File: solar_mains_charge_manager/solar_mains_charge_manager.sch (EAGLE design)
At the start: 11 parts, among them T1 TIP122, X1 22-23-2031, X2 22-23-2021, X4 22-23-2031, X5 22-23-2031

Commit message: Some more schematic and spreadsheet
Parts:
- added C1: (no value), capacitor-wima:C5/2.5
- added D1, D2, D3, D4: 1N4004, diode:1N4004
- added D5: (no value), diode:ZENER-DIODEDO34-7
- added OK2: PC817, optocoupler:PC817
- added R5: (no value), resistor:R-EU_0204/5
- added R6, R7, R8: (no value), resistor:R-EU_0204/7
- added X3: 22-23-2031, con-molex:22-23-2031
- added X6: 22-23-2041, con-molex:22-23-2041
- added X7, X8: 53047-15, con-molex:53047-15
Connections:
- new net N$10: D3.A, D4.A, D5.A, OK2.C
- new net N$11: D1.C, D2.C, R7.2
- new net N$12: OK2.COL, U$1.D12, X8-1.S
- new net N$13: C1.1, D1.A, D3.C, R8.1
- new net N$14: C1.2, R8.2
- new net N$15: D2.A, D4.C, R6.1
- new net N$16: R6.2
- new net N$17: U$1.D11, X3-2.S, X8-2.S
- new net N$18: U$1.D10, X3-3.S, X8-3.S
- new net N$19: U$1.D9, X6-3.S, X8-4.S
- new net N$20: U$1.D8, X6-4.S, X8-5.S
- new net N$21: U$1.RST, X6-2.S, X7-3.S
- new net N$22: U$1.D7, X8-6.S
- new net N$23: U$1.D6, X8-7.S
- new net N$24: U$1.D5, X8-8.S
- new net N$25: U$1.D4, X8-9.S
- new net N$26: U$1.D3, X8-10.S
- new net N$27: U$1.D2, X8-11.S
- new net N$28: U$1.GND2, X8-12.S
- new net N$29: U$1.RST1, X8-13.S
- new net N$30: U$1.RX1, X8-14.S
- new net N$31: U$1.TX0, X8-15.S
- new net N$32: U$1.5.5V, X7-4.S
- new net N$33: U$1.A7, X7-5.S
- new net N$34: U$1.A6, X7-6.S
- new net N$35: U$1.A5, X7-7.S
- new net N$36: U$1.A4, X7-8.S
- new net N$37: U$1.A3, X7-9.S
- new net N$38: U$1.A2, X7-10.S
- new net N$39: U$1.A1, X7-11.S
- new net N$8: OK2.A, R5.1
- new net N$9: D5.C, R5.2, R7.1
- net 12V: now also X7-1.S
- net GND: now also OK2.EMIT, X3-1.S, X6-1.S, X7-2.S
- net N$1: now also X7-13.S, X7-14.S
- net N$2: now also X7-15.S
- net N$3: now also X7-12.S

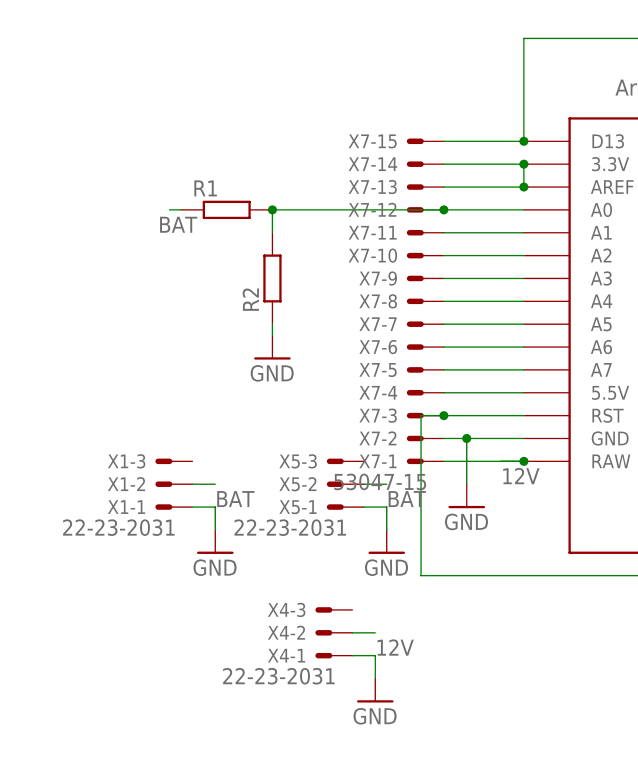
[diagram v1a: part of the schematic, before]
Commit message: Added solar panel voltage measurement along with over voltage and negative voltage protection in schematic, plus comments on the same in psu_considerations.ods
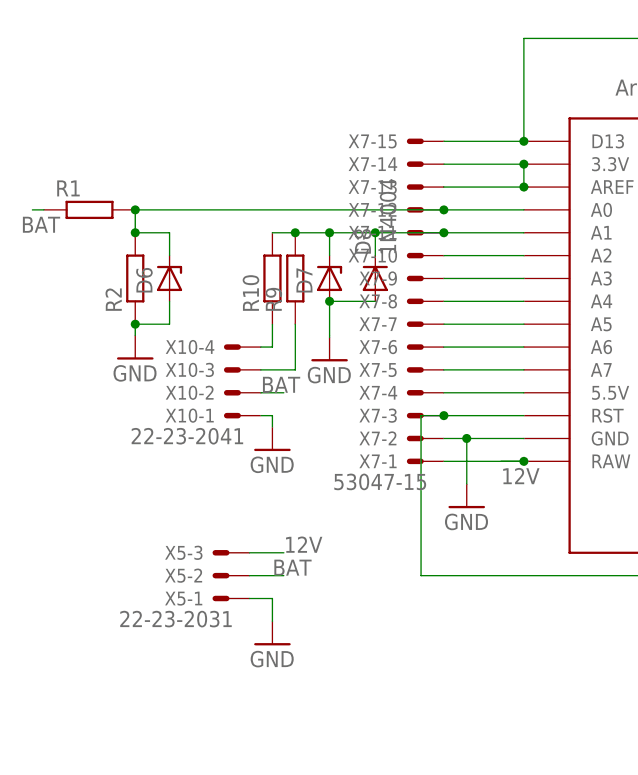
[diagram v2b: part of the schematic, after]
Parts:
- removed X1, X4: 22-23-2031, con-molex:22-23-2031
- added D6, D7: (no value), diode:ZENER-DIODEDO34-7
- added D8: 1N4004, diode:1N4004
- added R10, R9: (no value), resistor:R-EU_0204/5
- added X10: 22-23-2041, con-molex:22-23-2041
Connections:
- new net N$41: R10.1, X10-4.S
- new net N$42: R9.1, X10-3.S
- net 12V: now also X5-3.S; no longer X4-2.S
- net BAT: now also X10-2.S; no longer X1-2.S
- net GND: now also D6.A, D7.A, D8.A, X10-1.S; no longer X1-1.S, X4-1.S
- net N$3: now also D6.C
- net N$39: now also D7.C, D8.C, R10.2, R9.2
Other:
- moved on the sheet: R1, R2, X5-1, X5-2, X5-3

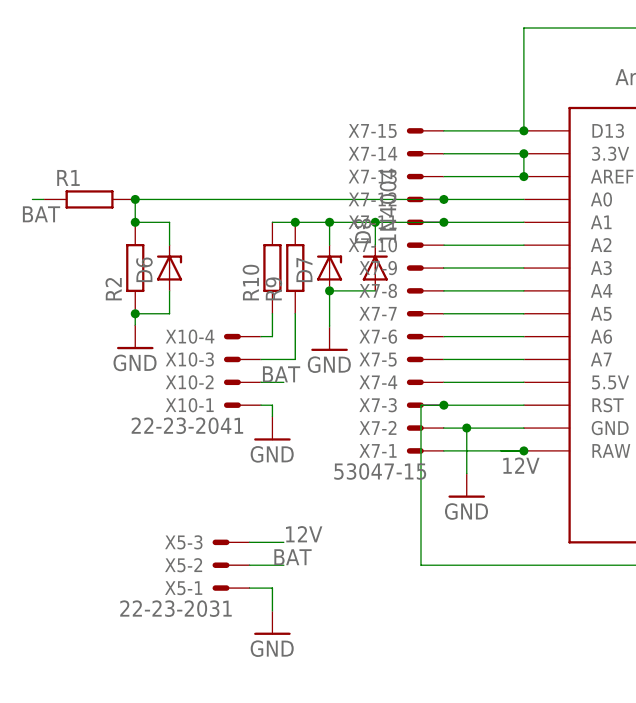
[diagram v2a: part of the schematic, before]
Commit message: Continued work on adding overvoltage protection on analog inputs and measurement of solar panel voltage
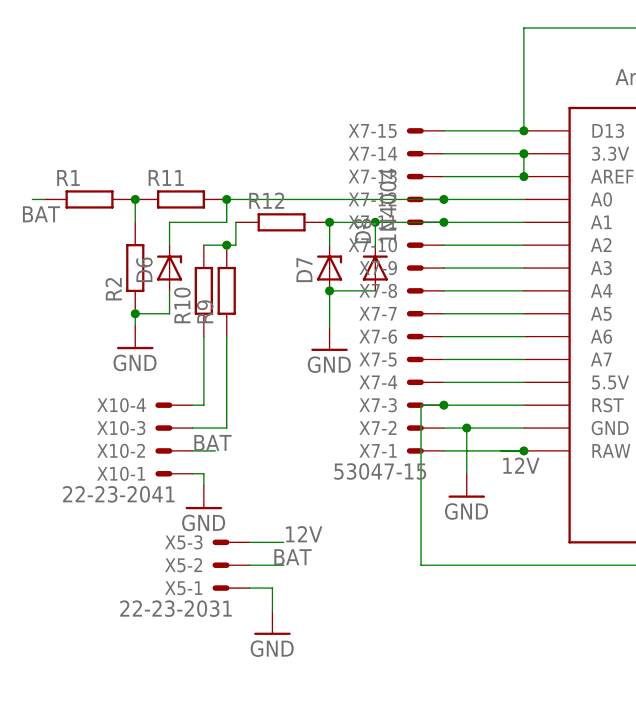
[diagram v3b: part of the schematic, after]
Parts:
- added R11, R12: (no value), resistor:R-EU_0204/5
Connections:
- new net N$40: D6.C, R11.2, U$1.A0, X7-12.S
- new net N$43: R1.2, R11.1, R2.2
- net N$3: now also R10.2, R12.1, R9.2; no longer D6.C, R1.2, R2.2, U$1.A0, X7-12.S
- net N$39: now also R12.2; no longer R10.2, R9.2
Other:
- moved on the sheet: R10, R9, X10-1, X10-2, X10-3, X10-4
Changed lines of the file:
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@@
 <setting verticaltext="up"/>
 </settings>
-<grid distance="0.1" unitdist="inch" unit="inch" style="lines" multiple="1" display="no" altdistance="0.01" altunitdist="inch" altunit="inch"/>
+<grid distance="0.01" unitdist="inch" unit="inch" style="lines" multiple="1" display="no" altdistance="0.01" altunitdist="inch" altunit="inch"/>
 <layers>
 <layer number="1" name="Top" color="4" fill="1" visible="no" active="no"/>
@@
 <part name="GND4" library="supply1" library_urn="urn:adsk.eagle:library:371" deviceset="GND" device=""/>
 <part name="D8" library="diode" library_urn="urn:adsk.eagle:library:210" deviceset="1N4004" device="" package3d_urn="urn:adsk.eagle:package:43336/1"/>
+<part name="R11" library="resistor" library_urn="urn:adsk.eagle:library:348" deviceset="R-EU_" device="0204/5" package3d_urn="urn:adsk.eagle:package:25955/1"/>
+<part name="R12" library="resistor" library_urn="urn:adsk.eagle:library:348" deviceset="R-EU_" device="0204/5" package3d_urn="urn:adsk.eagle:package:25955/1"/>
 </parts>
 <sheets>
@@
 <instance part="X8" gate="-14" x="121.92" y="55.88"/>
 <instance part="X8" gate="-15" x="121.92" y="53.34"/>
-<instance part="R9" gate="G$1" x="59.69" y="73.66" rot="R90"/>
-<instance part="R10" gate="G$1" x="57.15" y="73.66" rot="R90"/>
-<instance part="X10" gate="-1" x="53.34" y="58.42" rot="R180"/>
-<instance part="X10" gate="-2" x="53.34" y="60.96" rot="R180"/>
-<instance part="X10" gate="-3" x="53.34" y="63.5" rot="R180"/>
-<instance part="X10" gate="-4" x="53.34" y="66.04" rot="R180"/>
-<instance part="GND11" gate="1" x="57.15" y="54.61"/>
+<instance part="R9" gate="G$1" x="52.07" y="71.12" rot="R90"/>
+<instance part="R10" gate="G$1" x="49.53" y="71.12" rot="R90"/>
+<instance part="X10" gate="-1" x="45.72" y="50.8" rot="R180"/>
+<instance part="X10" gate="-2" x="45.72" y="53.34" rot="R180"/>
+<instance part="X10" gate="-3" x="45.72" y="55.88" rot="R180"/>
+<instance part="X10" gate="-4" x="45.72" y="58.42" rot="R180"/>
+<instance part="GND11" gate="1" x="49.53" y="46.99"/>
 <instance part="D6" gate="G$1" x="45.72" y="73.66" rot="R90"/>
 <instance part="D7" gate="G$1" x="63.5" y="73.66" rot="R90"/>
 <instance part="GND4" gate="1" x="63.498146875" y="64.573690625"/>
 <instance part="D8" gate="1" x="68.58" y="73.66" rot="R90"/>
+<instance part="R11" gate="G$1" x="46.99" y="81.28"/>
+<instance part="R12" gate="G$1" x="58.166" y="78.74"/>
 </instances>
 <busses>
@@
 </segment>
 </net>
-<net name="N$3" class="0">
-<segment>
-<pinref part="R2" gate="G$1" pin="2"/>
-<pinref part="R1" gate="G$1" pin="2"/>
-<wire x1="41.91" y1="81.28" x2="41.91" y2="78.74" width="0.1524" layer="91"/>
-<pinref part="U$1" gate="G$1" pin="A0"/>
-<wire x1="41.91" y1="81.28" x2="76.2" y2="81.28" width="0.1524" layer="91"/>
-<junction x="41.91" y="81.28"/>
-<pinref part="X7" gate="-12" pin="S"/>
-<wire x1="76.2" y1="81.28" x2="85.09" y2="81.28" width="0.1524" layer="91"/>
-<junction x="76.2" y="81.28"/>
-<pinref part="D6" gate="G$1" pin="C"/>
-<wire x1="41.91" y1="78.74" x2="45.72" y2="78.74" width="0.1524" layer="91"/>
-<wire x1="45.72" y1="78.74" x2="45.72" y2="76.2" width="0.1524" layer="91"/>
-<junction x="41.91" y="78.74"/>
-</segment>
-</net>
 <net name="GND" class="0">
 <segment>
@@
 <pinref part="X10" gate="-1" pin="S"/>
 <pinref part="GND11" gate="1" pin="GND"/>
-<wire x1="55.88" y1="58.42" x2="57.15" y2="58.42" width="0.1524" layer="91"/>
-<wire x1="57.15" y1="58.42" x2="57.15" y2="57.15" width="0.1524" layer="91"/>
+<wire x1="48.26" y1="50.8" x2="49.53" y2="50.8" width="0.1524" layer="91"/>
+<wire x1="49.53" y1="50.8" x2="49.53" y2="49.53" width="0.1524" layer="91"/>
 </segment>
 <segment>
@@
 <segment>
 <pinref part="X10" gate="-2" pin="S"/>
-<wire x1="55.88" y1="60.96" x2="58.42" y2="60.96" width="0.1524" layer="91"/>
-<label x="55.88" y="60.96" size="1.778" layer="95"/>
+<wire x1="48.26" y1="53.34" x2="50.8" y2="53.34" width="0.1524" layer="91"/>
+<label x="48.26" y="53.34" size="1.778" layer="95"/>
 </segment>
 </net>
@@
 <pinref part="U$1" gate="G$1" pin="A1"/>
 <wire x1="76.2" y1="78.74" x2="85.09" y2="78.74" width="0.1524" layer="91"/>
-<pinref part="R9" gate="G$1" pin="2"/>
 <wire x1="76.2" y1="78.74" x2="68.58" y2="78.74" width="0.1524" layer="91"/>
 <junction x="76.2" y="78.74"/>
-<pinref part="R10" gate="G$1" pin="2"/>
 <wire x1="68.58" y1="78.74" x2="63.5" y2="78.74" width="0.1524" layer="91"/>
-<wire x1="63.5" y1="78.74" x2="59.69" y2="78.74" width="0.1524" layer="91"/>
-<wire x1="59.69" y1="78.74" x2="57.15" y2="78.74" width="0.1524" layer="91"/>
-<junction x="59.69" y="78.74"/>
 <pinref part="D7" gate="G$1" pin="C"/>
 <wire x1="63.5" y1="76.2" x2="63.5" y2="78.74" width="0.1524" layer="91"/>
-<junction x="63.5" y="78.74"/>
 <pinref part="D8" gate="1" pin="C"/>
 <wire x1="68.58" y1="76.2" x2="68.58" y2="78.74" width="0.1524" layer="91"/>
 <junction x="68.58" y="78.74"/>
+<pinref part="R12" gate="G$1" pin="2"/>
+<wire x1="63.246" y1="78.74" x2="63.5" y2="78.74" width="0.1524" layer="91"/>
+<junction x="63.5" y="78.74"/>
 </segment>
 </net>
@@
 <pinref part="X10" gate="-4" pin="S"/>
 <pinref part="R10" gate="G$1" pin="1"/>
-<wire x1="55.88" y1="66.04" x2="57.15" y2="66.04" width="0.1524" layer="91"/>
-<wire x1="57.15" y1="66.04" x2="57.15" y2="68.58" width="0.1524" layer="91"/>
+<wire x1="48.26" y1="58.42" x2="49.53" y2="58.42" width="0.1524" layer="91"/>
+<wire x1="49.53" y1="58.42" x2="49.53" y2="66.04" width="0.1524" layer="91"/>
 </segment>
 </net>
@@
 <pinref part="X10" gate="-3" pin="S"/>
 <pinref part="R9" gate="G$1" pin="1"/>
-<wire x1="55.88" y1="63.5" x2="59.69" y2="63.5" width="0.1524" layer="91"/>
-<wire x1="59.69" y1="63.5" x2="59.69" y2="68.58" width="0.1524" layer="91"/>
-</segment>
-</net>
+<wire x1="48.26" y1="55.88" x2="52.07" y2="55.88" width="0.1524" layer="91"/>
+<wire x1="52.07" y1="55.88" x2="52.07" y2="66.04" width="0.1524" layer="91"/>
+</segment>
+</net>
+<net name="N$40" class="0">
+<segment>
+<pinref part="D6" gate="G$1" pin="C"/>
+<wire x1="45.72" y1="78.74" x2="45.72" y2="76.2" width="0.1524" layer="91"/>
+<pinref part="R11" gate="G$1" pin="2"/>
+<wire x1="45.72" y1="78.74" x2="52.07" y2="78.74" width="0.1524" layer="91"/>
+<wire x1="52.07" y1="78.74" x2="52.07" y2="81.28" width="0.1524" layer="91"/>
+<pinref part="U$1" gate="G$1" pin="A0"/>
+<pinref part="X7" gate="-12" pin="S"/>
+<wire x1="76.2" y1="81.28" x2="85.09" y2="81.28" width="0.1524" layer="91"/>
+<wire x1="52.07" y1="81.28" x2="76.2" y2="81.28" width="0.1524" layer="91"/>
+<junction x="52.07" y="81.28"/>
+<junction x="76.2" y="81.28"/>
+</segment>
+</net>
+<net name="N$43" class="0">
+<segment>
+<pinref part="R2" gate="G$1" pin="2"/>
+<pinref part="R1" gate="G$1" pin="2"/>
+<wire x1="41.91" y1="81.28" x2="41.91" y2="78.74" width="0.1524" layer="91"/>
+<pinref part="R11" gate="G$1" pin="1"/>
+<junction x="41.91" y="81.28"/>
+</segment>
+</net>
+<net name="N$3" class="0">
+<segment>
+<pinref part="R10" gate="G$1" pin="2"/>
+<pinref part="R9" gate="G$1" pin="2"/>
+<wire x1="52.07" y1="76.2" x2="49.53" y2="76.2" width="0.1524" layer="91"/>
+<pinref part="R12" gate="G$1" pin="1"/>
+<wire x1="53.086" y1="78.74" x2="53.086" y2="76.2" width="0.1524" layer="91"/>
+<wire x1="53.086" y1="76.2" x2="52.07" y2="76.2" width="0.1524" layer="91"/>
+<junction x="52.07" y="76.2"/>
+</segment>
+</net>

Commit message: A lot of stuff
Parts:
- removed C1: (no value), capacitor-wima:C5/2.5
- removed D1, D2, D3, D4, D8: 1N4004, diode:1N4004
- removed D5, D6, D7: (no value), diode:ZENER-DIODEDO34-7
- removed OK1, OK2: PC817, optocoupler:PC817
- removed R1, R10, R11, R12, R2, R3, R4, R5, R9: (no value), resistor:R-EU_0204/5
- removed R6, R7, R8: (no value), resistor:R-EU_0204/7
- removed T1: TIP122, transistor:TIP122
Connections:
- removed net N$1: U$1.3.3V, U$1.AREF, X7-13.S, X7-14.S
- removed net N$10: D3.A, D4.A, D5.A, OK2.C
- removed net N$11: D1.C, D2.C, R7.2
- removed net N$13: C1.1, D1.A, D3.C, R8.1
- removed net N$14: C1.2, R8.2
- removed net N$15: D2.A, D4.C, R6.1
- removed net N$16: R6.2
- removed net N$3: R10.2, R12.1, R9.2
- removed net N$4: OK1.A, R3.1
- removed net N$43: R1.2, R11.1, R2.2
- removed net N$6: OK1.EMIT, R4.1
- removed net N$7: R4.2, T1.B
- removed net N$8: OK2.A, R5.1
- removed net N$9: D5.C, R5.2, R7.1
- new net 12V1: U$1.AREF, X2-1.S, X7-13.S
- net 12V: no longer OK1.COL, X2-1.S
- net BAT: no longer R1.1
- net GND: no longer D6.A, D7.A, D8.A, OK1.C, OK2.EMIT, R2.1, T1.E
- net N$12: no longer OK2.COL
- net N$2: no longer R3.2
- net N$39: no longer D7.C, D8.C, R12.2
- net N$40: no longer D6.C, R11.2
- net N$41: no longer R10.1
- net N$42: no longer R9.1
- net N$5: now also U$1.3.3V, X7-14.S; no longer T1.C
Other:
- moved on the sheet: X2-1, X2-2

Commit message: Stuff
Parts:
- removed X10, X6: 22-23-2041, con-molex:22-23-2041
- removed X3, X5: 22-23-2031, con-molex:22-23-2031
- removed X7, X8: 53047-15, con-molex:53047-15
- added C1, C2, C6: (no value), capacitor-wima:C2,5-3
- added D1: (no value), diode:ZENER-DIODEDO34-7
- added F-1: (no value), qfm-trx1-24g:FUSE
- added JMP1, JMP2, JMP3: 0R-JUMPA, jump-0r-smd:0R-JUMPA
- added R1, R11, R12, R13, R14, R15, R16, R17: (no value), rcl:R-US_0204/5
- added R10, R2, R3, R4, R5, R6, R7, R8, R9: (no value), resistor:R-US_0204/2V
- added R19: (no value), resistor:R-EU_0204/5
- added S1, S2, S3: (no value), switch-omron:10-XX
- added SJ1, SJ10, SJ11, SJ12: (no value), jumper:SJ
- added SV1, SV2: (no value), con-lsta:FE15-1
- added SV3, SV8: (no value), con-lstb:MA04-1
- added SV4, SV5, SV6, SV7: (no value), con-lstb:MA07-1
- added SV9: (no value), con-lstb:MA03-1
- added TIP122: IRF530, transistor-power:IRF530
- added V-REG-1: (no value), qfm-trx1-24g:MCP1702
- added X1: 22-23-2021, con-molex:22-23-2021
- U$1: device Arduino-clone:NANO -> nano_without_those_headers:NANO
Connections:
- removed net 12V: U$1.RAW, X5-3.S, X7-1.S
- removed net 12V1: U$1.AREF, X2-1.S, X7-13.S
- removed net N$17: U$1.D11, X3-2.S, X8-2.S
- removed net N$19: U$1.D9, X6-3.S, X8-4.S
- removed net N$22: U$1.D7, X8-6.S
- removed net N$23: U$1.D6, X8-7.S
- removed net N$27: U$1.D2, X8-11.S
- removed net N$28: U$1.GND2, X8-12.S
- removed net N$32: U$1.5.5V, X7-4.S
- removed net N$33: U$1.A7, X7-5.S
- removed net N$34: U$1.A6, X7-6.S
- removed net N$35: U$1.A5, X7-7.S
- removed net N$36: U$1.A4, X7-8.S
- removed net N$37: U$1.A3, X7-9.S
- removed net N$38: U$1.A2, X7-10.S
- removed net N$39: U$1.A1, X7-11.S
- removed net N$40: U$1.A0, X7-12.S
- removed net N$41: X10-4.S
- removed net N$42: X10-3.S
- new net 5V: SJ1.1, SJ12.2, SV1.4, SV3.3, SV6.1, SV6.2, SV6.3, SV6.4, SV6.5, SV6.6, SV6.7, SV8.3, SV9.3, U$1.5.5V
- new net A0: R1.2, R8.1, U$1.A0
- new net A1: R11.2, R7.1, U$1.A1
- new net A2: R12.2, R6.1, U$1.A2
- new net A3: R13.2, R5.1, U$1.A3
- new net A4: JMP3-0R.1, R14.2, R4.1, U$1.A4
- new net A5: JMP2-0R.1, R15.2, R3.1, U$1.A5
- new net A6: R10.1, R16.2, U$1.A6
- new net A7: R17.2, R9.1, SV9.1, U$1.A7
- new net AREF: SJ1.2, SV1.13, U$1.AREF
- new net D8: S2.S, SV2.5, U$1.D8
- new net D9: S1.S1, SV2.4, U$1.D9
- new net N$1: C1.1, R19.2, SJ11.1, TIP122.S
- new net N$13: JMP3-0R.2, SV3.1
- new net N$3: C6.1, D1.C, R19.1, R2.2, TIP122.G
- new net N$4: SV2.1, U$1.D12
- new net N$6: JMP1-0R.3, V-REG-1.P$1
- new net N$7: SV2.2, U$1.D11
- new net N$8: F-1.P$1, X2-2.S
- new net RELAY: SV2.7, U$1.D6, X1-2.S
- new net RST: S3.S1, SV1.3, U$1.RST
- new net SCLSW: JMP2-0R.3, SV2.11, U$1.D2
- new net SDASW: JMP3-0R.3, SV2.6, U$1.D7
- new net VD0: R8.2, SJ10.2, SV1.12
- new net VD1: R7.2, SV1.11
- new net VD2: R6.2, SV1.10
- new net VD3: R5.2, SV1.9
- new net VD4: R4.2, SV1.8
- new net VD5: R3.2, SV1.7
- new net VD6: R10.2, SV1.6
- new net VD7: R9.2, SV1.5
- new net VIN: JMP1-0R.1, SV1.1, U$1.RAW
- net BAT: now also F-1.P$2, R2.1, SJ10.1, SV4.1, SV4.2, SV4.3, SV4.4, SV4.5, SV4.6, SV4.7, SV8.1, TIP122.D; no longer X10-2.S, X5-2.S
- net GND: now also C1.2, C2.2, C6.2, D1.A, R1.1, R11.1, R12.1, R13.1, R14.1, R15.1, R16.1, R17.1, S1.P1, S2.P1, S3.P1, SV1.2, SV2.12, SV3.4, SV7.1, SV7.2, SV7.3, SV7.4, SV7.5, SV7.6, SV7.7, SV8.4, SV9.2, U$1.GND2, V-REG-1.P$2, X1-1.S, X2-1.S; no longer X10-1.S, X3-1.S, X5-1.S, X6-1.S, X7-2.S
- net N$12: now also JMP2-0R.2, SV3.2; no longer U$1.D12, X8-1.S
- net N$18: now also SV2.3; no longer X3-3.S, X8-3.S
- net N$2: now also SV1.15; no longer X7-15.S
- net N$20: now also C2.1, SJ12.1, V-REG-1.P$3; no longer U$1.D8, X6-4.S, X8-5.S
- net N$21: now also JMP1-0R.2, SJ11.2, SV5.1, SV5.2, SV5.3, SV5.4, SV5.5, SV5.6, SV5.7, SV8.2; no longer U$1.RST, X6-2.S, X7-3.S
- net N$24: now also SV2.8; no longer X8-8.S
- net N$25: now also SV2.9; no longer X8-9.S
- net N$26: now also SV2.10; no longer X8-10.S
- net N$29: now also SV2.13; no longer X8-13.S
- net N$30: now also SV2.14; no longer X8-14.S
- net N$31: now also SV2.15; no longer X8-15.S
- net N$5: now also SV1.14; no longer X2-2.S, X7-14.S
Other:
- moved on the sheet: X2-1, X2-2
